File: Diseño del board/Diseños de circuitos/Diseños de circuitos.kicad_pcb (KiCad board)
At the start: 2 copper layers, 89.8 x 54.8 mm, 4 parts

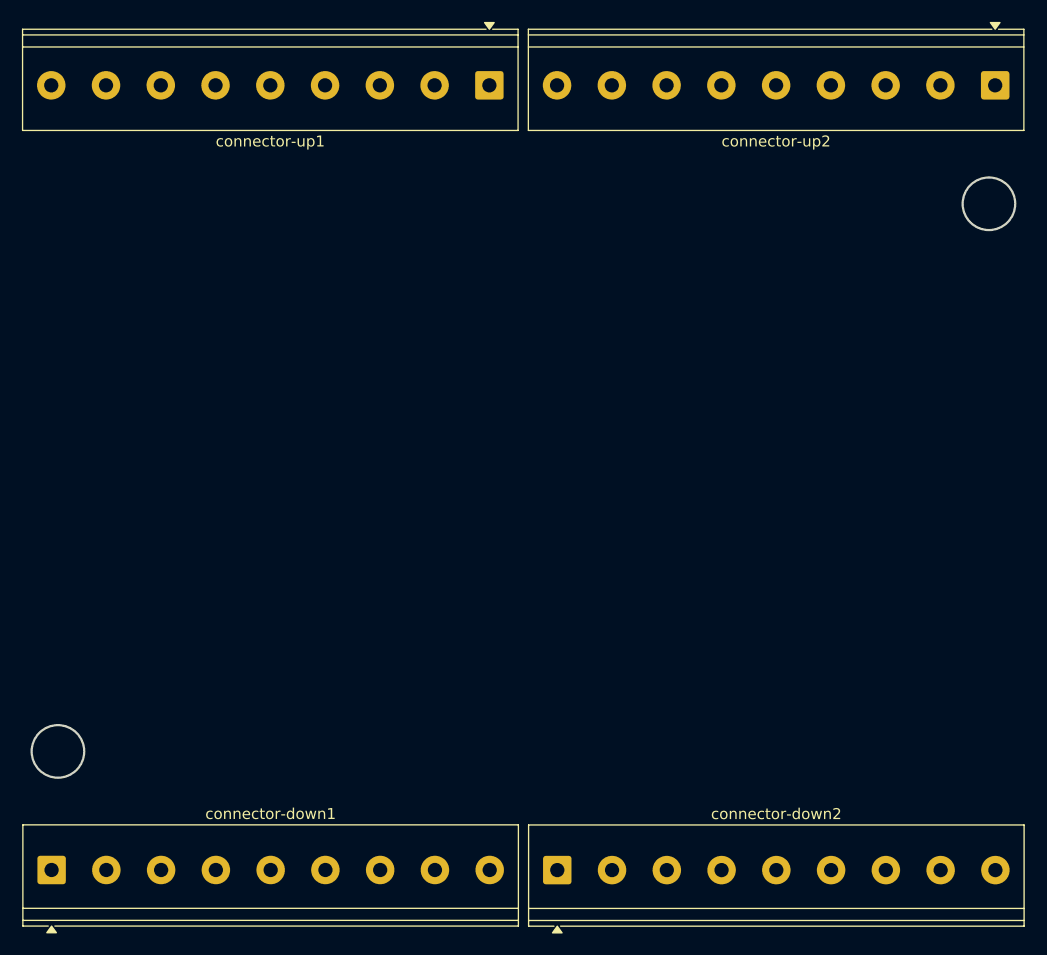
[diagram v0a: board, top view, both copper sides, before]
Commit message: se agrego entrada y salida 0-10V
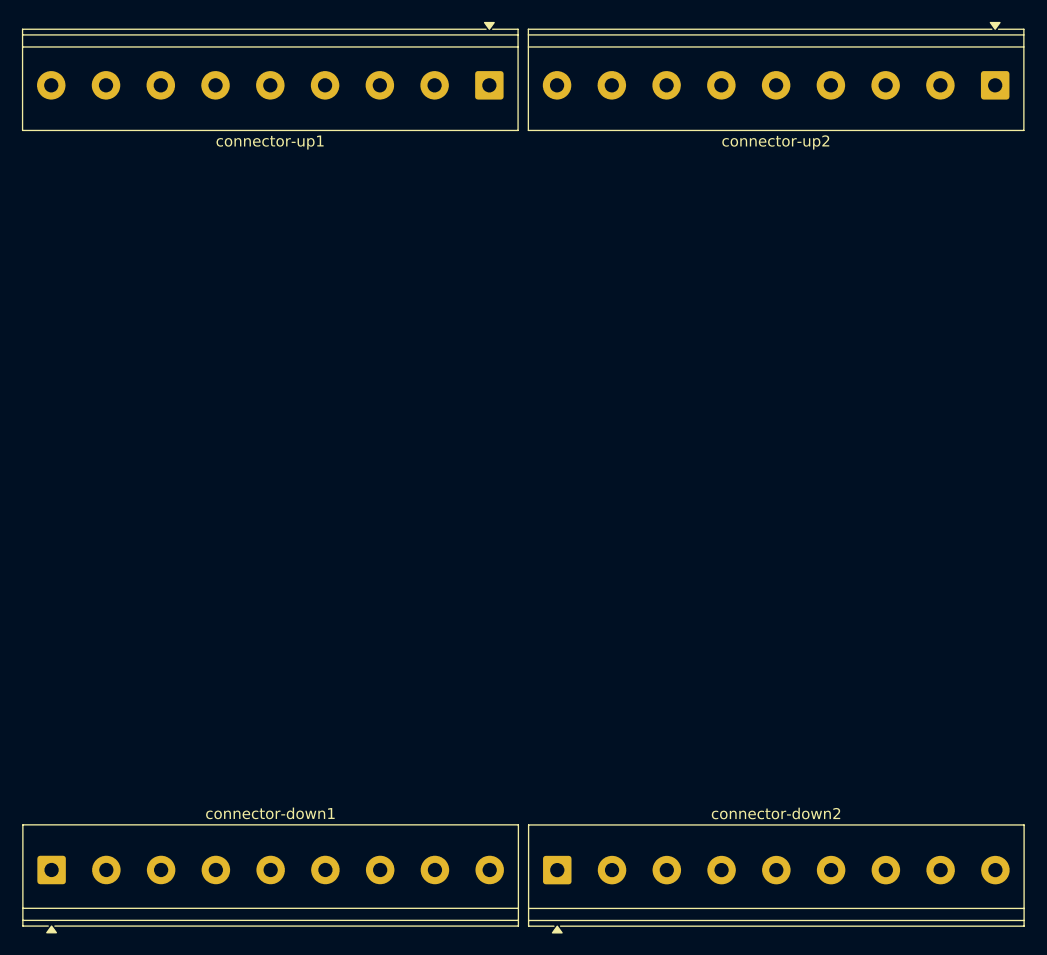
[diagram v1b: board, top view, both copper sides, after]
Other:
- board outline removed
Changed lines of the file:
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@@
 		)
+	)
+	(gr_line
+		(start 132.72 143.485)
+		(end 90.62 143.485)
+		(stroke
+			(width 0.2032)
+			(type default)
+		)
+		(layer "User.4")
+	)
+	(gr_line
+		(start 192.82 143.485)
+		(end 192.82 121.785)
+		(stroke
+			(width 0.2032)
+			(type default)
+		)
+		(layer "User.4")
+	)
+	(gr_line
+		(start 90.62 82.285)
+		(end 90.62 60.585)
+		(stroke
+			(width 0.2032)
+			(type default)
+		)
+		(layer "User.4")
 	)
 	(gr_circle
@@
 		)
 		(fill no)
-		(layer "Edge.Cuts")
+		(layer "User.4")
+	)
+	(gr_line
+		(start 90.62 82.285)
+		(end 90.62 60.585)
+		(stroke
+			(width 0.2032)
+			(type default)
+		)
+		(layer "User.4")
+	)
+	(gr_line
+		(start 90.62 96.435)
+		(end 92.07 96.435)
+		(stroke
+			(width 0.2032)
+			(type default)
+		)
+		(layer "User.4")
+	)
+	(gr_line
+		(start 191.37 96.435)
+		(end 191.37 99.535)
+		(stroke
+			(width 0.2032)
+			(type default)
+		)
+		(layer "User.4")
+	)
+	(gr_line
+		(start 90.62 82.285)
+		(end 90.62 60.585)
+		(stroke
+			(width 0.2032)
+			(type default)
+		)
+		(layer "User.4")
+	)
+	(gr_line
+		(start 90.62 143.535)
+		(end 192.82 143.535)
+		(stroke
+			(width 0.2032)
+			(type default)
+		)
+		(layer "User.4")
+	)
+	(gr_line
+		(start 192.82 143.485)
+		(end 192.82 121.785)
+		(stroke
+			(width 0.2032)
+			(type default)
+		)
+		(layer "User.4")
+	)
+	(gr_line
+		(start 90.62 96.435)
+		(end 92.07 96.435)
+		(stroke
+			(width 0.2032)
+			(type default)
+		)
+		(layer "User.4")
+	)
+	(gr_line
+		(start 92.07 96.435)
+		(end 92.07 99.535)
+		(stroke
+			(width 0.2032)
+			(type default)
+		)
+		(layer "User.4")
+	)
+	(gr_line
+		(start 92.07 104.535)
+		(end 92.07 107.635)
+		(stroke
+			(width 0.2032)
+			(type default)
+		)
+		(layer "User.4")
+	)
+	(gr_line
+		(start 191.37 107.635)
+		(end 192.82 107.635)
+		(stroke
+			(width 0.2032)
+			(type default)
+		)
+		(layer "User.4")
+	)
+	(gr_line
+		(start 192.82 96.435)
+		(end 191.37 96.435)
+		(stroke
+			(width 0.2032)
+			(type default)
+		)
+		(layer "User.4")
+	)
+	(gr_line
+		(start 191.37 107.635)
+		(end 192.82 107.635)
+		(stroke
+			(width 0.2032)
+			(type default)
+		)
+		(layer "User.4")
+	)
+	(gr_line
+		(start 92.07 96.435)
+		(end 92.07 99.535)
+		(stroke
+			(width 0.2032)
+			(type default)
+		)
+		(layer "User.4")
+	)
+	(gr_line
+		(start 92.07 96.435)
+		(end 92.07 104.535)
+		(stroke
+			(width 0.2032)
+			(type default)
+		)
+		(layer "User.4")
+	)
+	(gr_line
+		(start 92.07 107.635)
+		(end 90.62 107.635)
+		(stroke
+			(width 0.2032)
+			(type default)
+		)
+		(layer "User.4")
+	)
+	(gr_line
+		(start 90.62 143.485)
+		(end 90.62 121.785)
+		(stroke
+			(width 0.2032)
+			(type default)
+		)
+		(layer "User.4")
+	)
+	(gr_line
+		(start 192.82 143.485)
+		(end 192.82 121.785)
+		(stroke
+			(width 0.2032)
+			(type default)
+		)
+		(layer "User.4")
+	)
+	(gr_line
+		(start 191.37 96.435)
+		(end 191.37 107.635)
+		(stroke
+			(width 0.2032)
+			(type default)
+		)
+		(layer "User.4")
+	)
+	(gr_line
+		(start 92.07 107.635)
+		(end 90.62 107.635)
+		(stroke
+			(width 0.2032)
+			(type default)
+		)
+		(layer "User.4")
+	)
+	(gr_line
+		(start 191.37 107.635)
+		(end 192.82 107.635)
+		(stroke
+			(width 0.2032)
+			(type default)
+		)
+		(layer "User.4")
+	)
+	(gr_line
+		(start 192.82 96.435)
+		(end 191.37 96.435)
+		(stroke
+			(width 0.2032)
+			(type default)
+		)
+		(layer "User.4")
 	)
 	(gr_circle
@@
 		)
 		(fill no)
-		(layer "Edge.Cuts")
-	)
-	(gr_line
-		(start 132.72 143.485)
-		(end 90.62 143.485)
-		(stroke
-			(width 0.2032)
-			(type default)
-		)
-		(layer "User.4")
-	)
-	(gr_line
-		(start 192.82 143.485)
-		(end 192.82 121.785)
-		(stroke
-			(width 0.2032)
-			(type default)
-		)
-		(layer "User.4")
-	)
-	(gr_line
-		(start 90.62 82.285)
-		(end 90.62 60.585)
-		(stroke
-			(width 0.2032)
-			(type default)
-		)
-		(layer "User.4")
-	)
-	(gr_line
-		(start 90.62 82.285)
-		(end 90.62 60.585)
-		(stroke
-			(width 0.2032)
-			(type default)
-		)
-		(layer "User.4")
-	)
-	(gr_line
-		(start 90.62 96.435)
-		(end 92.07 96.435)
-		(stroke
-			(width 0.2032)
-			(type default)
-		)
-		(layer "User.4")
-	)
-	(gr_line
-		(start 191.37 96.435)
-		(end 191.37 99.535)
-		(stroke
-			(width 0.2032)
-			(type default)
-		)
-		(layer "User.4")
-	)
-	(gr_line
-		(start 90.62 82.285)
-		(end 90.62 60.585)
-		(stroke
-			(width 0.2032)
-			(type default)
-		)
-		(layer "User.4")
-	)
-	(gr_line
-		(start 90.62 143.535)
-		(end 192.82 143.535)
-		(stroke
-			(width 0.2032)
-			(type default)
-		)
-		(layer "User.4")
-	)
-	(gr_line
-		(start 192.82 143.485)
-		(end 192.82 121.785)
-		(stroke
-			(width 0.2032)
-			(type default)
-		)
-		(layer "User.4")
-	)
-	(gr_line
-		(start 90.62 96.435)
-		(end 92.07 96.435)
-		(stroke
-			(width 0.2032)
-			(type default)
-		)
-		(layer "User.4")
-	)
-	(gr_line
-		(start 92.07 96.435)
-		(end 92.07 99.535)
-		(stroke
-			(width 0.2032)
-			(type default)
-		)
-		(layer "User.4")
-	)
-	(gr_line
-		(start 92.07 104.535)
-		(end 92.07 107.635)
-		(stroke
-			(width 0.2032)
-			(type default)
-		)
-		(layer "User.4")
-	)
-	(gr_line
-		(start 191.37 107.635)
-		(end 192.82 107.635)
-		(stroke
-			(width 0.2032)
-			(type default)
-		)
-		(layer "User.4")
-	)
-	(gr_line
-		(start 192.82 96.435)
-		(end 191.37 96.435)
-		(stroke
-			(width 0.2032)
-			(type default)
-		)
-		(layer "User.4")
-	)
-	(gr_line
-		(start 191.37 107.635)
-		(end 192.82 107.635)
-		(stroke
-			(width 0.2032)
-			(type default)
-		)
-		(layer "User.4")
-	)
-	(gr_line
-		(start 92.07 96.435)
-		(end 92.07 99.535)
-		(stroke
-			(width 0.2032)
-			(type default)
-		)
-		(layer "User.4")
-	)
-	(gr_line
-		(start 92.07 96.435)
-		(end 92.07 104.535)
-		(stroke
-			(width 0.2032)
-			(type default)
-		)
-		(layer "User.4")
-	)
-	(gr_line
-		(start 92.07 107.635)
-		(end 90.62 107.635)
-		(stroke
-			(width 0.2032)
-			(type default)
-		)
-		(layer "User.4")
-	)
-	(gr_line
-		(start 90.62 143.485)
-		(end 90.62 121.785)
-		(stroke
-			(width 0.2032)
-			(type default)
-		)
-		(layer "User.4")
-	)
-	(gr_line
-		(start 192.82 143.485)
-		(end 192.82 121.785)
-		(stroke
-			(width 0.2032)
-			(type default)
-		)
-		(layer "User.4")
-	)
-	(gr_line
-		(start 191.37 96.435)
-		(end 191.37 107.635)
-		(stroke
-			(width 0.2032)
-			(type default)
-		)
-		(layer "User.4")
-	)
-	(gr_line
-		(start 92.07 107.635)
-		(end 90.62 107.635)
-		(stroke
-			(width 0.2032)
-			(type default)
-		)
-		(layer "User.4")
-	)
-	(gr_line
-		(start 191.37 107.635)
-		(end 192.82 107.635)
-		(stroke
-			(width 0.2032)
-			(type default)
-		)
-		(layer "User.4")
-	)
-	(gr_line
-		(start 192.82 96.435)
-		(end 191.37 96.435)
-		(stroke
-			(width 0.2032)
-			(type default)
-		)
-		(layer "User.4")
-	)
+		(layer "User.4")
+	)
